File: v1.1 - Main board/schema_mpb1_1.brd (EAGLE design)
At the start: 85.3 x 70.8 mm, 79 parts, among them IC1 CP2102, Q1 8M, Q2 32.768kHz, U1 NCP1117ST33T3G, U2 NCP1117ST50T3G, X2 PN61729-S, X5 POWERSUPPLY_DC21MMX

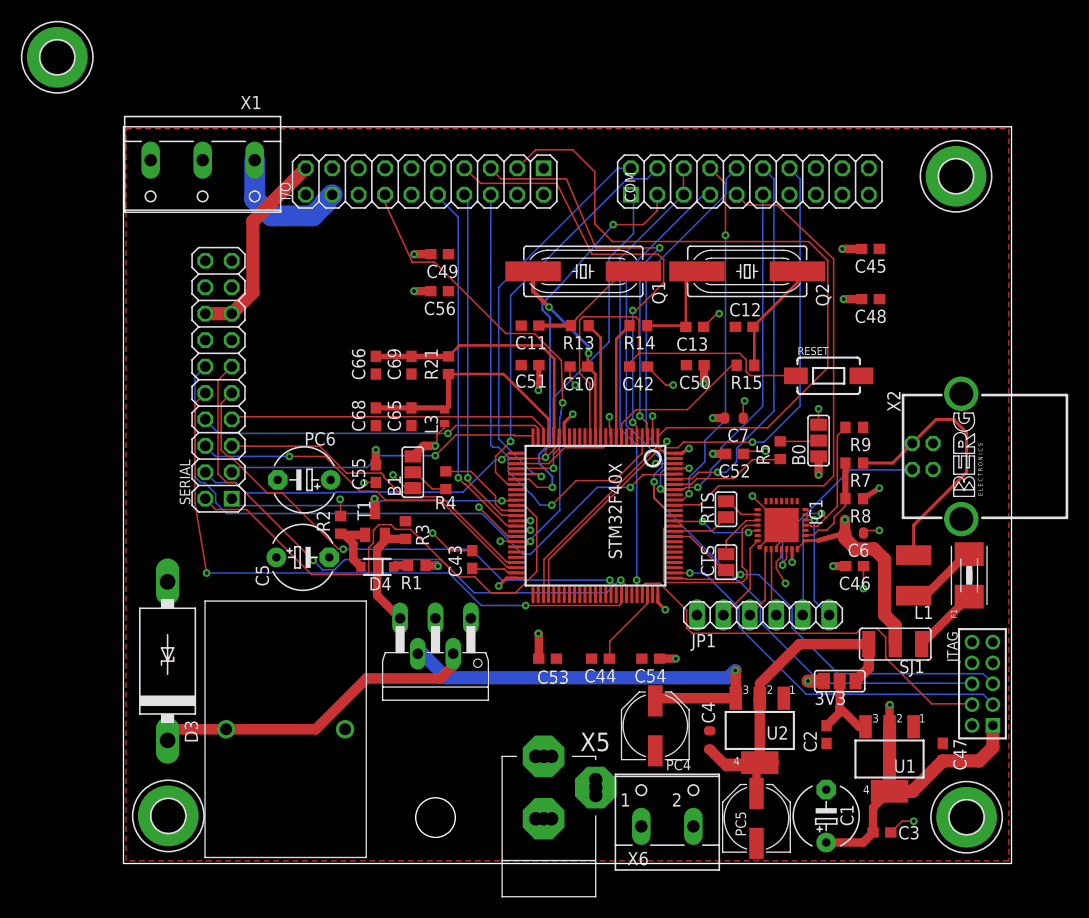
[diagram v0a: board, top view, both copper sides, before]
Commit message: Main board
- Rounded corners (2.54mm setting)
- Placed final mounting pad
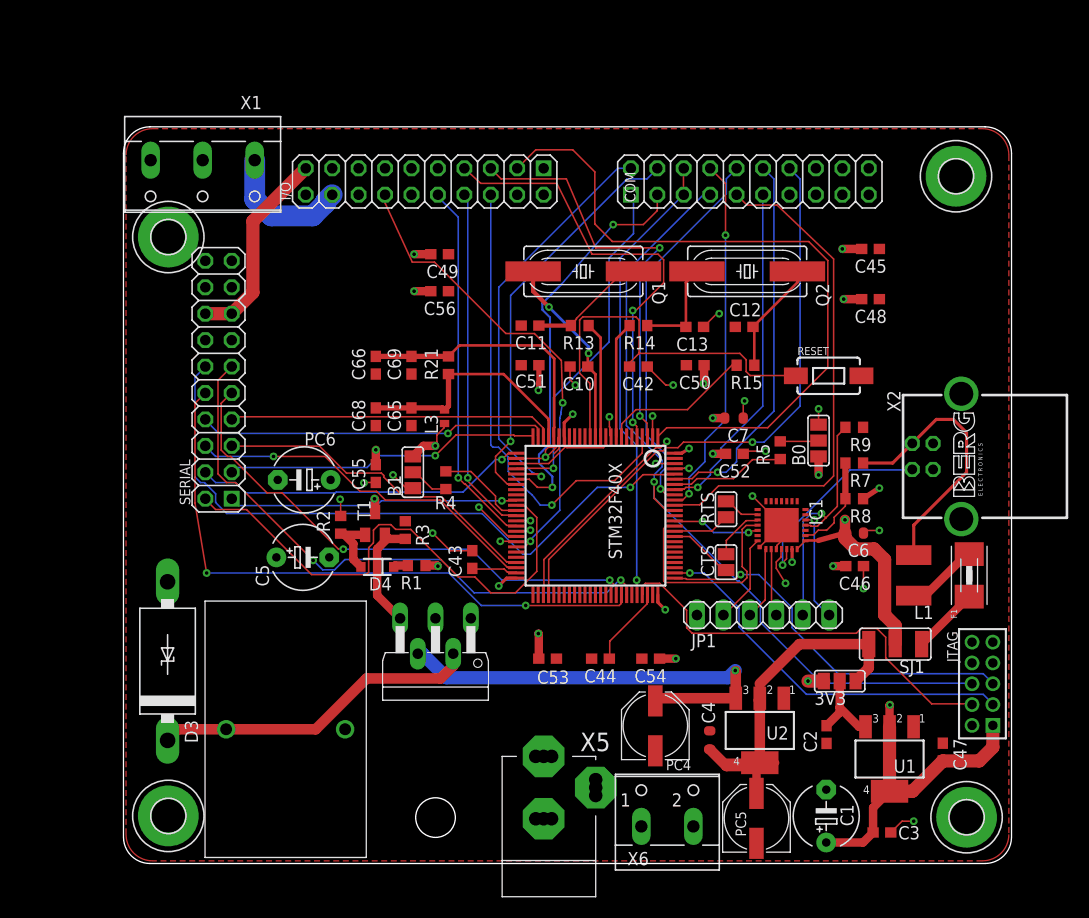
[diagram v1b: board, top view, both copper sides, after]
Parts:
- moved H3 20.3 mm to (4.57, 60.5)
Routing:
- net +12V: track 194.4 -> 153.7 mm
- net VIN: track 46.3 -> 47.8 mm
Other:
- outline, holes or cut-outs redrawn
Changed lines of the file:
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@@
 <board>
 <plain>
-<wire x1="85.598" y1="0.254" x2="85.598" y2="71.044" width="0" layer="20"/>
-<wire x1="85.598" y1="71.044" x2="0.264" y2="71.044" width="0" layer="20"/>
-<wire x1="0.264" y1="71.044" x2="0.264" y2="0.254" width="0" layer="20"/>
-<wire x1="0.264" y1="0.254" x2="85.598" y2="0.254" width="0" layer="20"/>
+<wire x1="0.264" y1="68.504" x2="0.264" y2="2.794" width="0" layer="20"/>
+<wire x1="0.264" y1="2.794" x2="2.804" y2="0.254" width="0" layer="20" curve="90"/>
+<wire x1="2.804" y1="0.254" x2="83.058" y2="0.254" width="0" layer="20"/>
+<wire x1="83.058" y1="0.254" x2="85.598" y2="2.794" width="0" layer="20" curve="90"/>
+<wire x1="85.598" y1="2.794" x2="85.598" y2="68.504" width="0" layer="20"/>
+<wire x1="85.598" y1="68.504" x2="83.058" y2="71.044" width="0" layer="20" curve="90"/>
+<wire x1="83.058" y1="71.044" x2="2.804" y2="71.044" width="0" layer="20"/>
+<wire x1="2.804" y1="71.044" x2="0.264" y2="68.504" width="0" layer="20" curve="90"/>
 <dimension x1="0" y1="-1.524" x2="85.598" y2="-1.524" x3="42.799" y3="-7.112" textsize="1.778" layer="21"/>
 <dimension x1="87.122" y1="0.254" x2="87.122" y2="70.866" x3="95.25" y3="35.56" textsize="1.778" layer="21"/>
@@
 <element name="H1" library="holes" library_urn="urn:adsk.eagle:library:237" package="3,2-PAD" package3d_urn="urn:adsk.eagle:package:14282/1" value="MOUNT-PAD-ROUND3.2" x="81.28" y="4.699" smashed="yes" rot="R90"/>
 <element name="H2" library="holes" library_urn="urn:adsk.eagle:library:237" package="3,2-PAD" package3d_urn="urn:adsk.eagle:package:14282/1" value="MOUNT-PAD-ROUND3.2" x="4.572" y="4.826" smashed="yes" rot="R90"/>
-<element name="H3" library="holes" library_urn="urn:adsk.eagle:library:237" package="3,2-PAD" package3d_urn="urn:adsk.eagle:package:14282/1" value="MOUNT-PAD-ROUND3.2" x="-6.096" y="77.724" smashed="yes" rot="R90"/>
+<element name="H3" library="holes" library_urn="urn:adsk.eagle:library:237" package="3,2-PAD" package3d_urn="urn:adsk.eagle:package:14282/1" value="MOUNT-PAD-ROUND3.2" x="4.572" y="60.452" smashed="yes" rot="R90"/>
 <element name="H4" library="holes" library_urn="urn:adsk.eagle:library:237" package="3,2-PAD" package3d_urn="urn:adsk.eagle:package:14282/1" value="MOUNT-PAD-ROUND3.2" x="80.264" y="66.294" smashed="yes" rot="R90"/>
 <element name="C1" library="adafruit" package="E5-6" value="1000uF" x="67.7926" y="4.812" smashed="yes" rot="R90">
@@
 <contactref element="B0" pad="3"/>
 <polygon width="0.6096" layer="2">
-<vertex x="85.217" y="0.635"/>
-<vertex x="0.635" y="0.635"/>
-<vertex x="0.635" y="70.739"/>
-<vertex x="85.217" y="70.739"/>
+<vertex x="85.217" y="68.199"/>
+<vertex x="85.217" y="3.175" curve="-90"/>
+<vertex x="82.677" y="0.635"/>
+<vertex x="3.175" y="0.635" curve="-90"/>
+<vertex x="0.635" y="3.175"/>
+<vertex x="0.635" y="68.199" curve="-90"/>
+<vertex x="3.175" y="70.739"/>
+<vertex x="82.677" y="70.739" curve="-90"/>
 </polygon>
 <contactref element="RESET" pad="2"/>
@@
 <contactref element="SERIAL" pad="14"/>
 <polygon width="0.3048" layer="1">
-<vertex x="85.344" y="0.508"/>
-<vertex x="0.508" y="0.508"/>
-<vertex x="0.508" y="70.866"/>
-<vertex x="85.344" y="70.866"/>
+<vertex x="85.344" y="68.326"/>
+<vertex x="85.344" y="3.048" curve="-90"/>
+<vertex x="82.804" y="0.508"/>
+<vertex x="3.048" y="0.508" curve="-90"/>
+<vertex x="0.508" y="3.048"/>
+<vertex x="0.508" y="68.326" curve="-90"/>
+<vertex x="3.048" y="70.866"/>
+<vertex x="82.804" y="70.866" curve="-90"/>
 </polygon>
 <contactref element="I/O" pad="15"/>
@@
 </polygon>
 <contactref element="I/O" pad="18"/>
-<wire x1="20.1686" y1="61.6194" x2="20.32" y2="64.516" width="2" layer="15"/>
 <wire x1="40.6376" y1="10.546" x2="40.6376" y2="13.9676" width="1.016" layer="15"/>
 <wire x1="40.6376" y1="13.9676" x2="40.64" y2="13.97" width="1.016" layer="15"/>
@@
 <wire x1="14.478" y1="62.484" x2="12.874" y2="64.088" width="2" layer="16"/>
 <wire x1="12.874" y1="64.088" x2="12.874" y2="67.838" width="2" layer="16"/>
-<wire x1="20.1686" y1="37.116" x2="20.1686" y2="61.6194" width="3" layer="15"/>
+<wire x1="20.1686" y1="37.116" x2="22.098" y2="39.0454" width="2" layer="15"/>
+<wire x1="20.32" y1="63.5" x2="20.32" y2="64.516" width="2" layer="15"/>
+<wire x1="22.098" y1="39.0454" x2="22.098" y2="61.722" width="2" layer="15"/>
+<wire x1="22.098" y1="61.722" x2="20.32" y2="63.5" width="2" layer="15"/>
+<wire x1="30.48" y1="28.702" x2="33.6444" y2="23.817" width="0" layer="19" extent="1-15"/>
+<wire x1="24.435" y1="34.0364" x2="29.2874" y2="28.888" width="0" layer="19" extent="1-1"/>
+<wire x1="22.098" y1="39.0454" x2="24.384" y2="35.306" width="0" layer="19" extent="1-15"/>
+<wire x1="40.6376" y1="13.9676" x2="33.6444" y2="23.817" width="0" layer="19" extent="1-15"/>
+<wire x1="50.0254" y1="3.82" x2="40.6376" y2="10.546" width="0" layer="19" extent="1-1"/>
 </signal>
 <signal name="+12V">
@@
 <wire x1="21.5616" y1="13.152" x2="14.9566" y2="19.757" width="4.2" layer="15"/>
 <wire x1="14.9566" y1="19.757" x2="14.9566" y2="29.672" width="4.2" layer="15"/>
-<wire x1="6.223" y1="31.496" x2="3.556" y2="34.163" width="2" layer="15"/>
-<wire x1="3.556" y1="34.163" x2="3.556" y2="58.166" width="2" layer="15"/>
-<wire x1="3.556" y1="58.166" x2="3.556" y2="59.182" width="2" layer="15"/>
 <wire x1="17.78" y1="64.516" x2="8.382" y2="64.516" width="2" layer="15"/>
-<wire x1="8.382" y1="64.516" x2="8.382" y2="64.262" width="2" layer="15"/>
-<wire x1="8.382" y1="64.262" x2="4.798965625" y2="60.490384375" width="2" layer="15"/>
 <contactref element="X1" pad="3"/>
-<wire x1="4.798965625" y1="60.490384375" x2="3.556" y2="59.182" width="2" layer="15"/>
-<wire x1="2.874" y1="67.838" x2="2.794" y2="61.976" width="2" layer="15"/>
-<wire x1="2.794" y1="61.976" x2="3.556" y2="58.166" width="2" layer="15"/>
 <wire x1="28.548" y1="20.4116" x2="28.9984125" y2="20.4116" width="1.27" layer="16"/>
 <wire x1="28.9984125" y1="20.4116" x2="31.3062125" y2="18.1038" width="1.27" layer="16"/>
@@
 <wire x1="28.548" y1="20.4116" x2="15.6112" y2="20.4116" width="3" layer="15"/>
 <wire x1="15.6112" y1="20.4116" x2="14.9566" y2="19.757" width="3" layer="15"/>
-<wire x1="2.874" y1="67.838" x2="2.874" y2="34.845" width="3" layer="15"/>
-<wire x1="2.874" y1="34.845" x2="6.223" y2="31.496" width="3" layer="15"/>
-<wire x1="6.223" y1="31.496" x2="13.1326" y2="31.496" width="3" layer="15"/>
-<wire x1="13.1326" y1="31.496" x2="14.9566" y2="29.672" width="3" layer="15"/>
+<wire x1="17.78" y1="64.516" x2="6.196" y2="64.516" width="2" layer="15"/>
+<wire x1="6.196" y1="64.516" x2="2.874" y2="67.838" width="2" layer="15"/>
+<wire x1="17.78" y1="64.516" x2="17.78" y2="36.068" width="2" layer="15"/>
+<wire x1="14.9566" y1="29.672" x2="14.9566" y2="33.2446" width="2" layer="15"/>
+<wire x1="14.9566" y1="33.2446" x2="17.78" y2="36.068" width="2" layer="15"/>
 </signal>
 <signal name="REG_5V">
@@
 <contactref element="C3" pad="1"/>
 <polygon width="0.6096" layer="15">
-<vertex x="85.217" y="0.635"/>
-<vertex x="0.635" y="0.635"/>
-<vertex x="0.635" y="70.739"/>
-<vertex x="85.217" y="70.739"/>
+<vertex x="85.217" y="68.199"/>
+<vertex x="85.217" y="3.175" curve="-90"/>
+<vertex x="82.677" y="0.635"/>
+<vertex x="3.175" y="0.635" curve="-90"/>
+<vertex x="0.635" y="3.175"/>
+<vertex x="0.635" y="68.199" curve="-90"/>
+<vertex x="3.175" y="70.739"/>
+<vertex x="82.677" y="70.739" curve="-90"/>
 </polygon>
 <contactref element="C55" pad="1"/>
@@
 <wire x1="22.987" y1="36.0172" x2="24.5872" y2="36.0172" width="0.1524" layer="1"/>
 <wire x1="19.6342" y1="39.37" x2="22.987" y2="36.0172" width="0.1524" layer="1"/>
-<wire x1="16.2052" y1="39.37" x2="19.6342" y2="39.37" width="0.1524" layer="1"/>
-<wire x1="9.1186" y1="39.37" x2="16.2052" y2="39.37" width="0.1524" layer="16"/>
+<wire x1="14.6812" y1="39.37" x2="19.6342" y2="39.37" width="0.1524" layer="1"/>
+<wire x1="9.1186" y1="39.37" x2="14.6812" y2="39.37" width="0.1524" layer="16"/>
 <wire x1="8.128" y1="40.3606" x2="9.1186" y2="39.37" width="0.1524" layer="16"/>
 <wire x1="37.9984" y1="28.702" x2="38.014796875" y2="28.67678125" width="0.1524" layer="1"/>
 <wire x1="8.128" y1="40.3606" x2="8.128" y2="40.386" width="0.1524" layer="16"/>
-<via x="16.2052" y="39.37" extent="1-16" drill="0.35"/>
+<via x="14.6812" y="39.37" extent="1-16" drill="0.35"/>
 </signal>
 <signal name="PC0">

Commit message: Main board
- Tidy routes
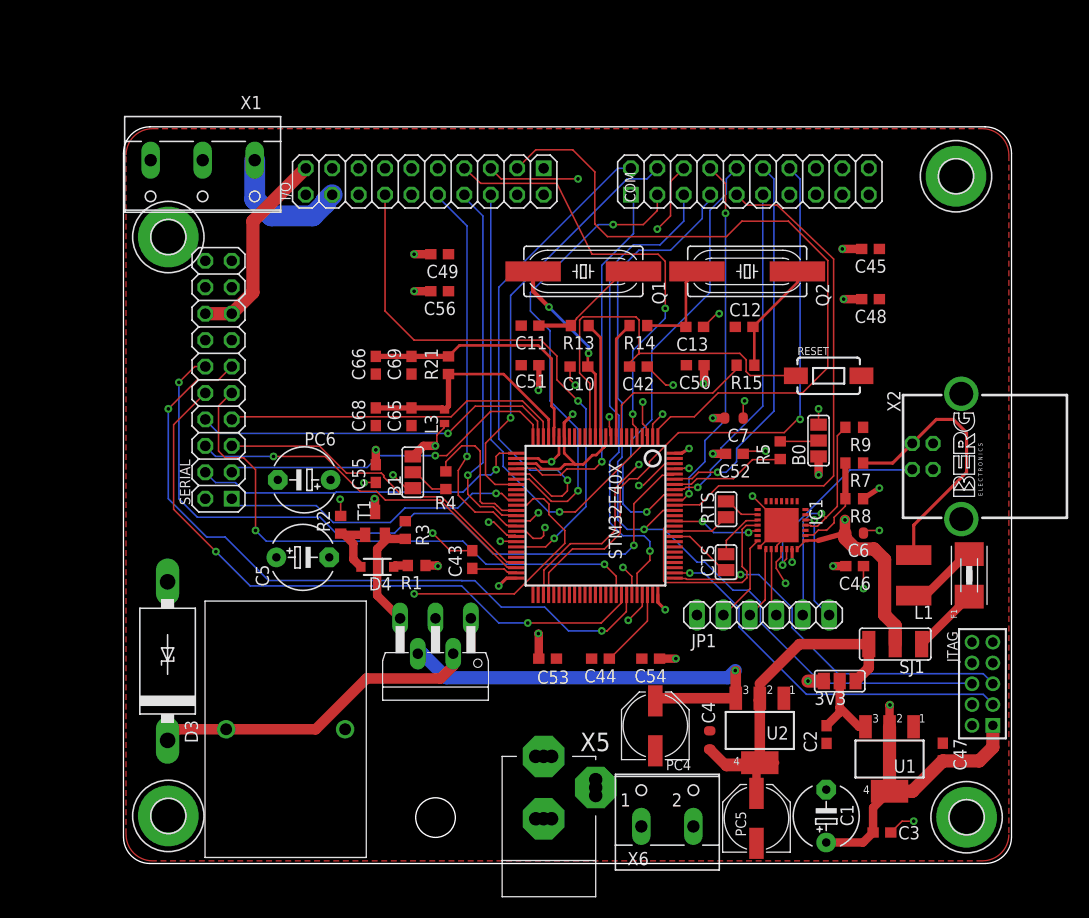
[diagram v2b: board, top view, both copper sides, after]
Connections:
- net CAN1_RX: now also COM.6
- net CAN1_TX: no longer COM.6
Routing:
- net CAN1_RX: track 0.00 -> 47.2 mm, vias 0 -> 2
- net TX6: track 57.3 -> 69.0 mm
- net PE13: track 45.5 -> 53.4 mm
- net RX6: track 63.9 -> 71.3 mm, vias 1 -> 2
- net ETH_SCK: track 40.0 -> 47.3 mm
- net ETH_MISO: track 39.3 -> 45.1 mm
- net NRF_CE: track 36.9 -> 42.7 mm
- net PE1: track 31.0 -> 36.6 mm
- net NRF_SCK: track 77.7 -> 83.2 mm
- net BOOT1: track 8.77 -> 13.7 mm
- net PE10: track 40.6 -> 45.2 mm
- net TX5: track 50.1 -> 54.5 mm
- net 3.3V: track 80.0 -> 84.3 mm
- net TMS/SWDIO: track 40.0 -> 44.3 mm, vias 0 -> 1
- net PE4: track 40.3 -> 44.0 mm
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
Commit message: Main board revisions
- Rerouted long tracks to other layers
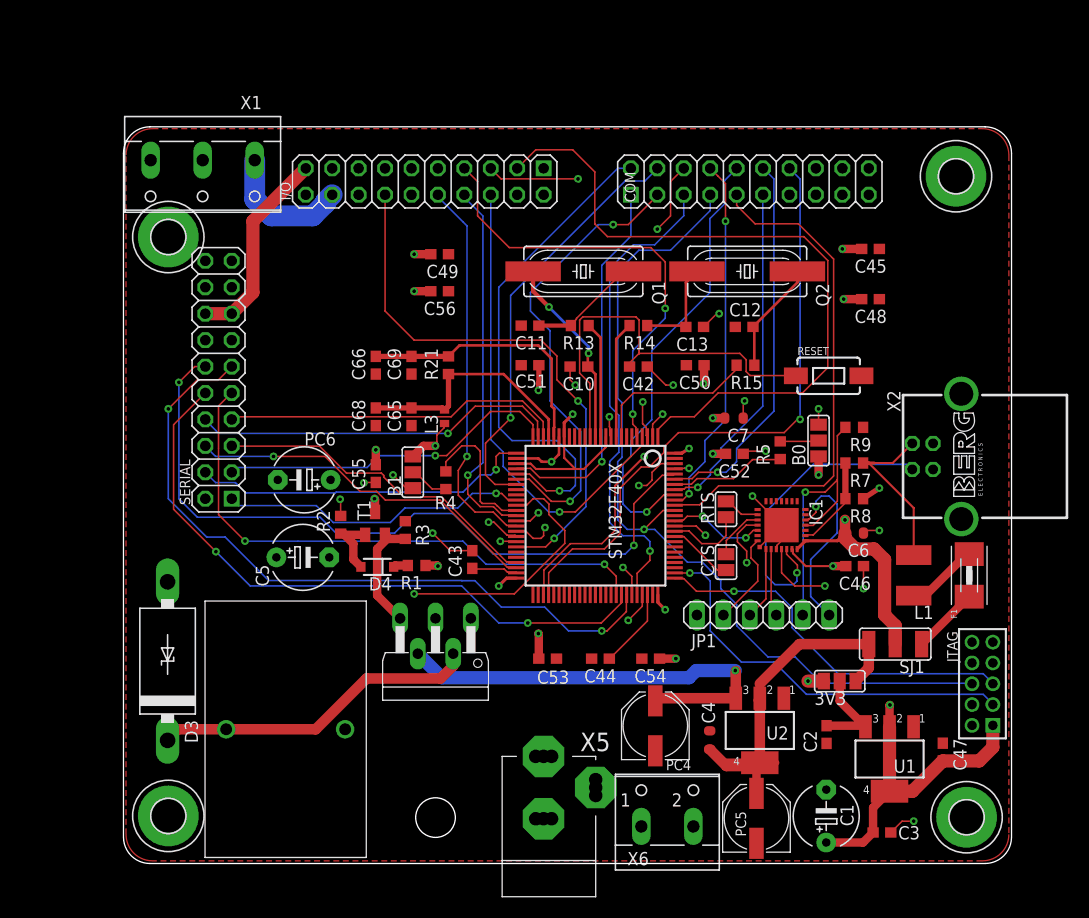
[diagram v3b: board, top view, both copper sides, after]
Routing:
- net N$17: track 26.1 -> 16.1 mm
- net N$13: track 19.5 -> 29.3 mm
- net N$26: track 10.6 -> 17.4 mm
- net +12V: track 153.7 -> 148.4 mm
- net N$21: track 23.5 -> 27.0 mm
- net USART2_TX: track 20.9 -> 17.8 mm, vias 0 -> 2
- net 3.3V: track 84.3 -> 86.5 mm, vias 20 -> 19
- net USART2_RTS: track 5.51 -> 7.56 mm
- net TDI: track 36.9 -> 38.7 mm
- net ETH_SCK: track 47.3 -> 48.6 mm
- net PE2: track 68.9 -> 67.7 mm
- net N$45: track 8.05 -> 9.19 mm
- net CAN1_RX: track 47.2 -> 46.2 mm
- net RX1: track 48.4 -> 49.5 mm
- net USB_OTG_HS_DM: track 50.7 -> 49.8 mm
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
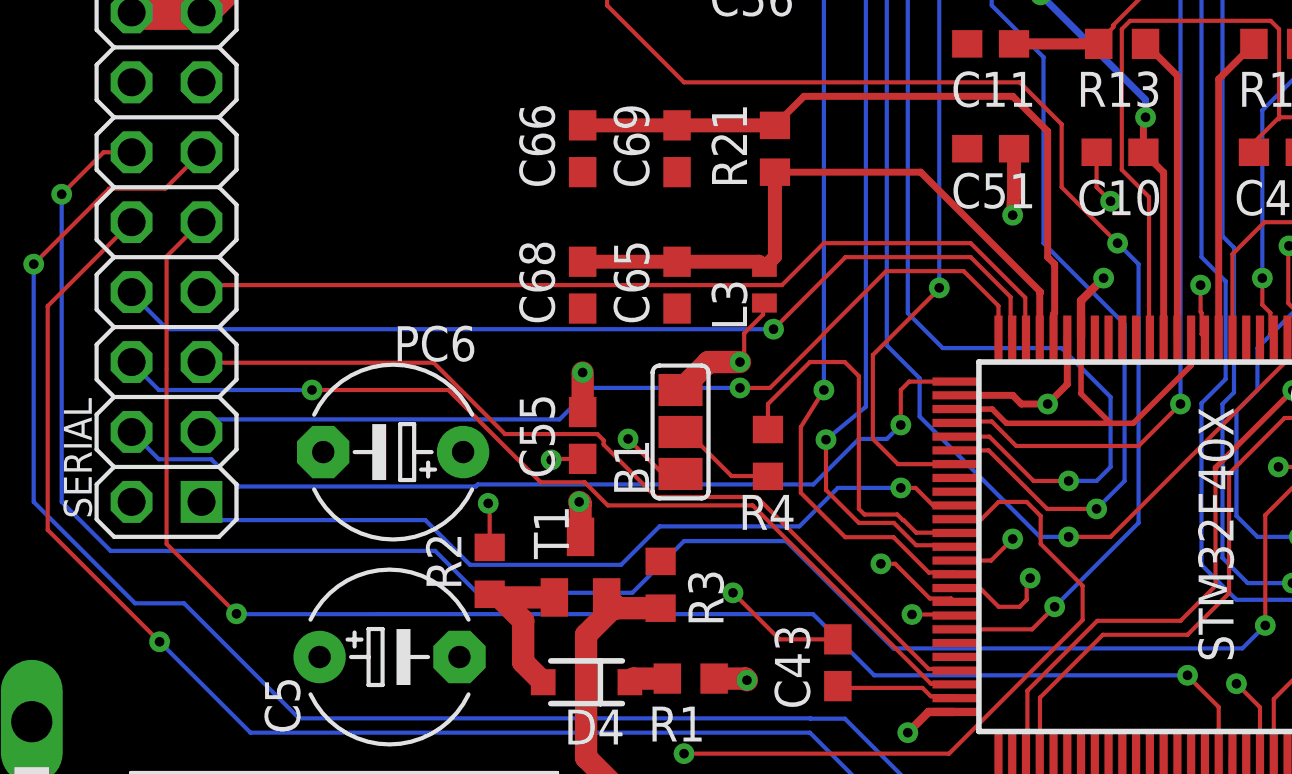
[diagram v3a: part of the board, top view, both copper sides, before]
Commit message: Main board
- Tidied tracks
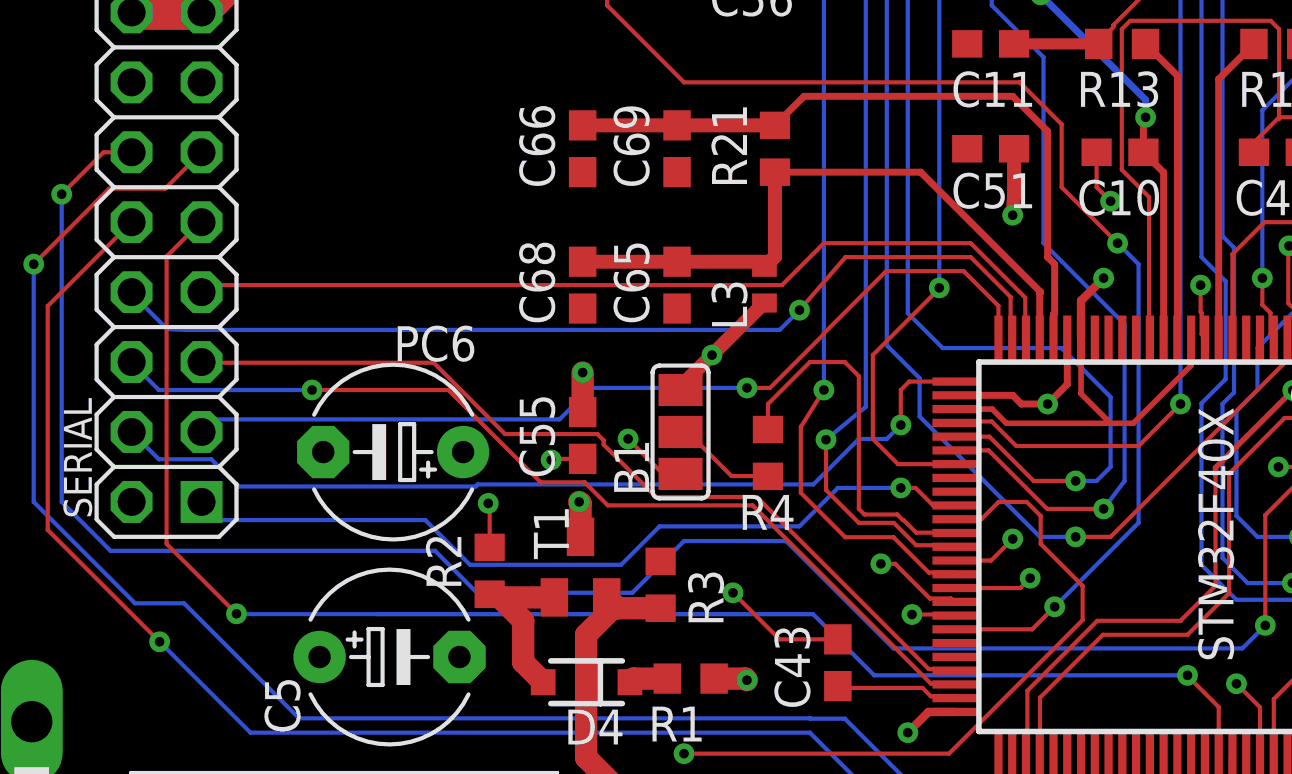
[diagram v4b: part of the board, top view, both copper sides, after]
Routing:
- net N$14: track 22.9 -> 23.6 mm
- net 3.3V: track 86.5 -> 85.9 mm
- net PE10: track 45.2 -> 44.7 mm
